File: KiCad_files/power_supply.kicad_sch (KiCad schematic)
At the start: 21 parts, among them Q2 DMP3099L, U7 LTC4412xS6

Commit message: power led
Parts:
- added D1: LED, LED_SMD:LED_0805_2012Metric_Pad1.15x1.40mm_HandSolder, symbol Device:LED
- added R1: 2.2k, Resistor_SMD:R_0805_2012Metric_Pad1.20x1.40mm_HandSolder, symbol Device:R
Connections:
- net +3.3V: now also R1.2
- net GND: now also D1.1 (K)
- new net: D1.2 (A), R1.1
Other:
- moved on the sheet: C17, C18, C19, C20, C21, C25, C26, C5, D2, D3, L5, Q2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

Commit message: digikey field for power supply components
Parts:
- removed L5: SRU1038-5R0Y, Inductor_SMD:L_Bourns-SRU1028_10.0x10.0mm, symbol 1_projektin osat:SRU1038-5R0Y
- added L4: SRU1038-5R0Y, 1_project_library:IND_BOURNS_SRU1038, symbol 1_projektin osat:SRU1038-5R0Y
- C17: DigiKey (none) -> 490-1644-1-ND
- C18, C19, C20: DigiKey (none) -> 720-1754-1-ND
- C21: DigiKey (none) -> 399-C0805C330J5GACTUCT-ND
- C5: DigiKey (none) -> 587-3246-1-ND
- D1: DigiKey (none) -> 492-2281-1-ND
- D2: DigiKey (none) -> CUS10S30H3FCT-ND
- D3: DigiKey (none) -> 1N4148WSFSCT-ND
- Q2: DigiKey (none) -> DMP3099L-7DICT-ND
- R1: DigiKey (none) -> 311-2.20KCRCT-ND
- R10: DigiKey (none) -> 311-100KCRCT-ND
- R11: DigiKey (none) -> 311-20.0CRCT-ND
- R12: DigiKey (none) -> 13-RC0805FR-135K6LCT-ND
- R13: DigiKey (none) -> 13-RT0805FRE0713KLCT-ND
- R14: DigiKey (none) -> 311-40.2KCRCT-ND
- R15: DigiKey (none) -> 311-470KCRCT-ND
- U7: DigiKey (none) -> 505-LTC4412ES6#TRMPBFCT-ND
- U8: DigiKey (none) -> 1589-1573-1-ND
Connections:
- net +3.3V: now also L4.1
- net at C19.1, U8.3 (SW): now also L4.2
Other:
- moved on the sheet: C19, R11

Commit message: c5 korjattu
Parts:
- renumbered C5 to C27
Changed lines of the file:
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@@
 		(dnp no)
 		(fields_autoplaced yes)
-		(property "Reference" "C5"
+		(property "Reference" "C27"
 			(at 231.14 101.5999 0)
 			(effects
@@
 			(project "esp"
 				(path "/186d5500-054c-4b47-a89c-85f6ce2abe33/718dca9f-314d-4628-afec-7956f3606013"
-					(reference "C5")
+					(reference "C27")
 					(unit 1)
 				)

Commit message: johtoja
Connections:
- net VBUS renamed USB_VBUS
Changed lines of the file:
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@@
 	(wire
 		(pts
-			(xy 201.93 95.25) (xy 205.74 95.25)
+			(xy 80.01 72.39) (xy 97.79 72.39)
 		)
 		(stroke
@@
 	(wire
 		(pts
-			(xy 185.42 80.01) (xy 175.26 80.01)
+			(xy 201.93 95.25) (xy 205.74 95.25)
 		)
 		(stroke
@@
 	(wire
 		(pts
-			(xy 218.44 110.49) (xy 227.33 110.49)
+			(xy 185.42 80.01) (xy 175.26 80.01)
 		)
 		(stroke
@@
 	(wire
 		(pts
-			(xy 223.52 81.28) (xy 223.52 95.25)
+			(xy 218.44 110.49) (xy 227.33 110.49)
 		)
 		(stroke
@@
 	(wire
 		(pts
-			(xy 218.44 106.68) (xy 218.44 110.49)
+			(xy 223.52 81.28) (xy 223.52 95.25)
 		)
 		(stroke
@@
 	(wire
 		(pts
-			(xy 124.46 72.39) (xy 124.46 77.47)
+			(xy 218.44 106.68) (xy 218.44 110.49)
 		)
 		(stroke
@@
 	(wire
 		(pts
-			(xy 91.44 72.39) (xy 97.79 72.39)
+			(xy 124.46 72.39) (xy 124.46 77.47)
 		)
 		(stroke
@@
 		)
 	)
+	(hierarchical_label "USB_VBUS"
+		(shape input)
+		(at 80.01 72.39 180)
+		(effects
+			(font
+				(size 1.27 1.27)
+			)
+			(justify right)
+		)
+	)
 	(hierarchical_label "BAT_STAT"
 		(shape output)
@@
 					(unit 1)
 				)
-			)
-		)
-	)
-	(symbol
-		(lib_id "power:VBUS")
-		(at 91.44 72.39 90)
-		(unit 1)
-		(exclude_from_sim no)
-		(in_bom yes)
-		(on_board yes)
-		(dnp no)
-		(fields_autoplaced yes)
-		(property "Reference" "#PWR021"
-			(at 95.25 72.39 0)
-			(effects
-				(font
-					(size 1.27 1.27)
-				)
-				(hide yes)
-			)
-		)
-		(property "Value" "VBUS"
-			(at 87.63 72.3899 90)
-			(effects
-				(font
-					(size 1.27 1.27)
-				)
-				(justify left)
-			)
-		)
-		(property "Footprint" ""
-			(at 91.44 72.39 0)
-			(effects
-				(font
-					(size 1.27 1.27)
-				)
-				(hide yes)
-			)
-		)
-		(property "Datasheet" ""
-			(at 91.44 72.39 0)
-			(effects
-				(font
-					(size 1.27 1.27)
-				)
-				(hide yes)
-			)
-		)
-		(property "Description" "Power symbol creates a global label with name \"VBUS\""
-			(at 91.44 72.39 0)
-			(effects
-				(font
-					(size 1.27 1.27)
-				)
-				(hide yes)
-			)
-		)
-		(pin "1"
-		)
-		(instances
-			(project ""
-				(path "/186d5500-054c-4b47-a89c-85f6ce2abe33/718dca9f-314d-4628-afec-7956f3606013"
-					(reference "#PWR021")
-					(unit 1)
-				)

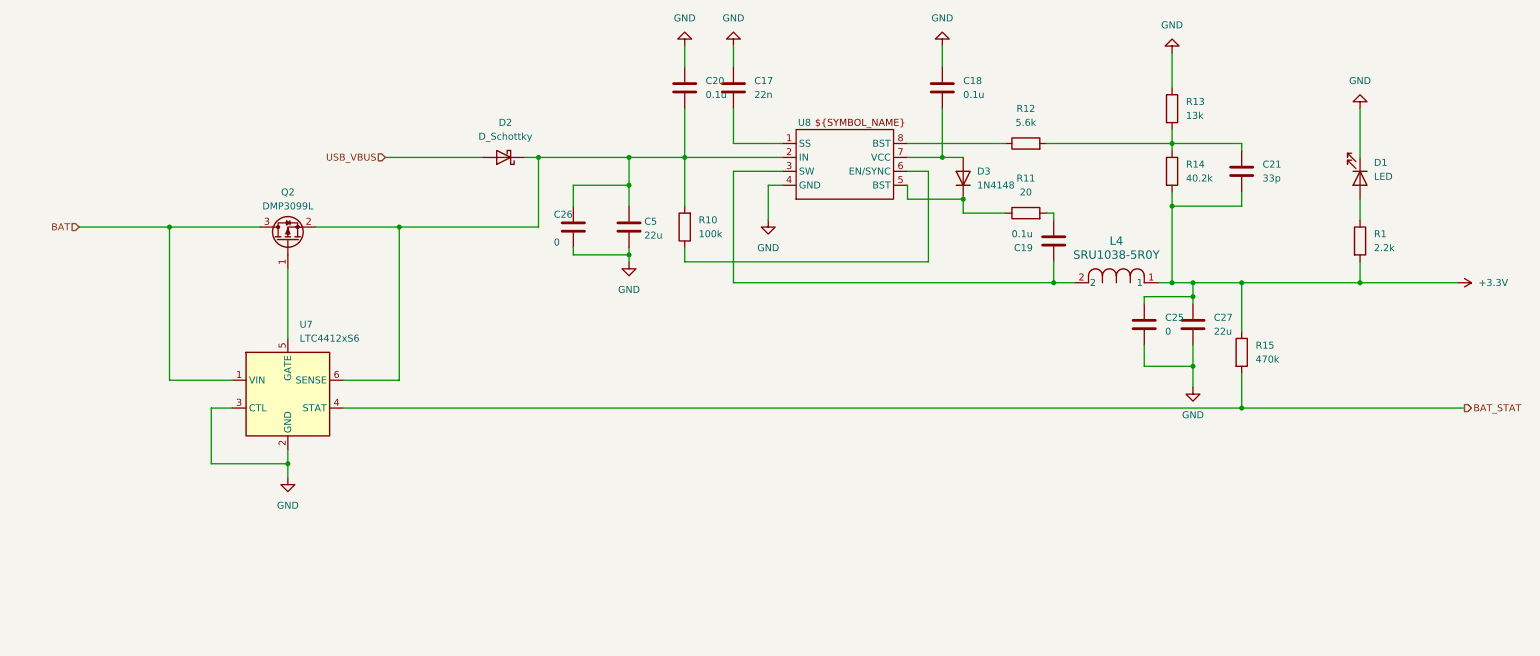
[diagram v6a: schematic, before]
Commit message: dpdt switch
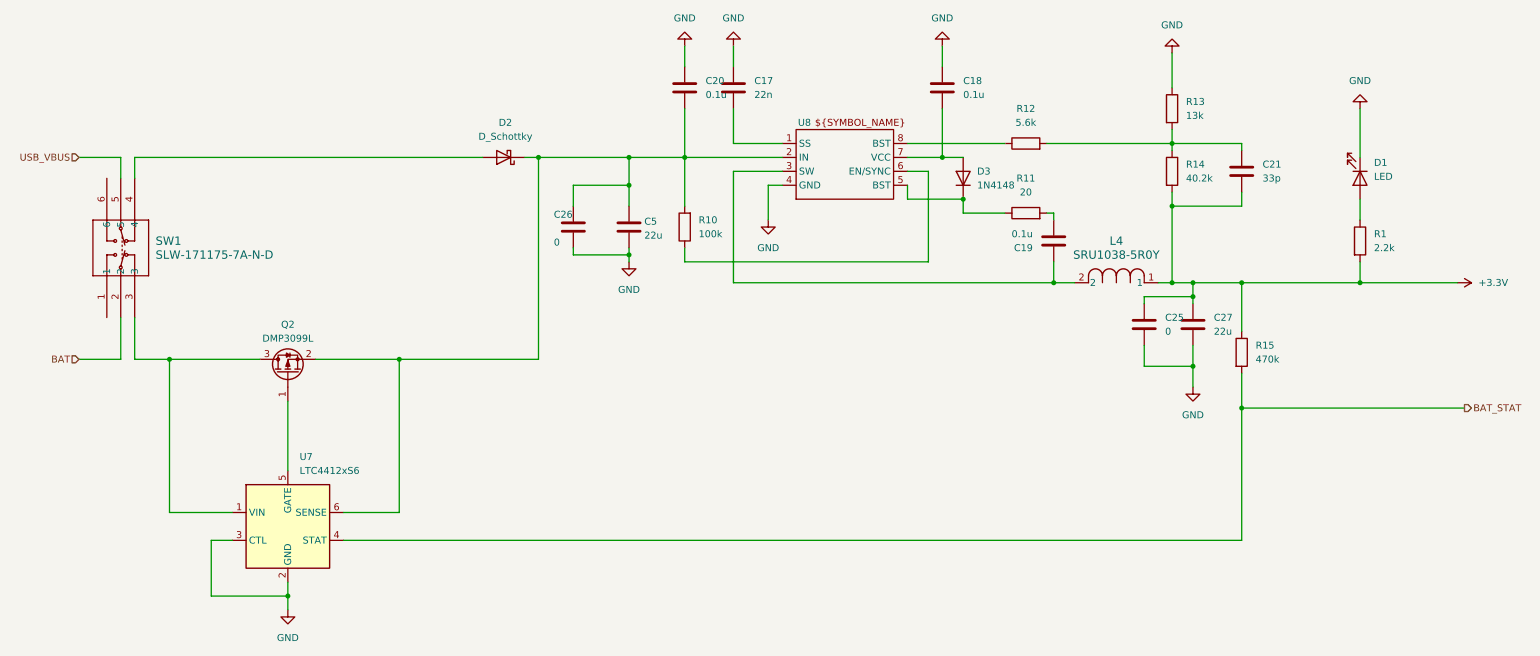
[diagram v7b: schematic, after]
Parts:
- added SW1: SLW-171175-7A-N-D, SLW-171175-7A-N-D_SSD, symbol 1_projektin osat:SLW-171175-7A-N-D
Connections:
- net BAT: now also SW1.2; no longer Q2.3 (D), U7.1 (VIN)
- net USB_VBUS: now also SW1.5; no longer D2.2 (A)
- new net: Q2.3 (D), SW1.3, U7.1 (VIN)
- new net: D2.2 (A), SW1.4
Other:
- moved on the sheet: Q2, U7

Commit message: ERC hiljennetty
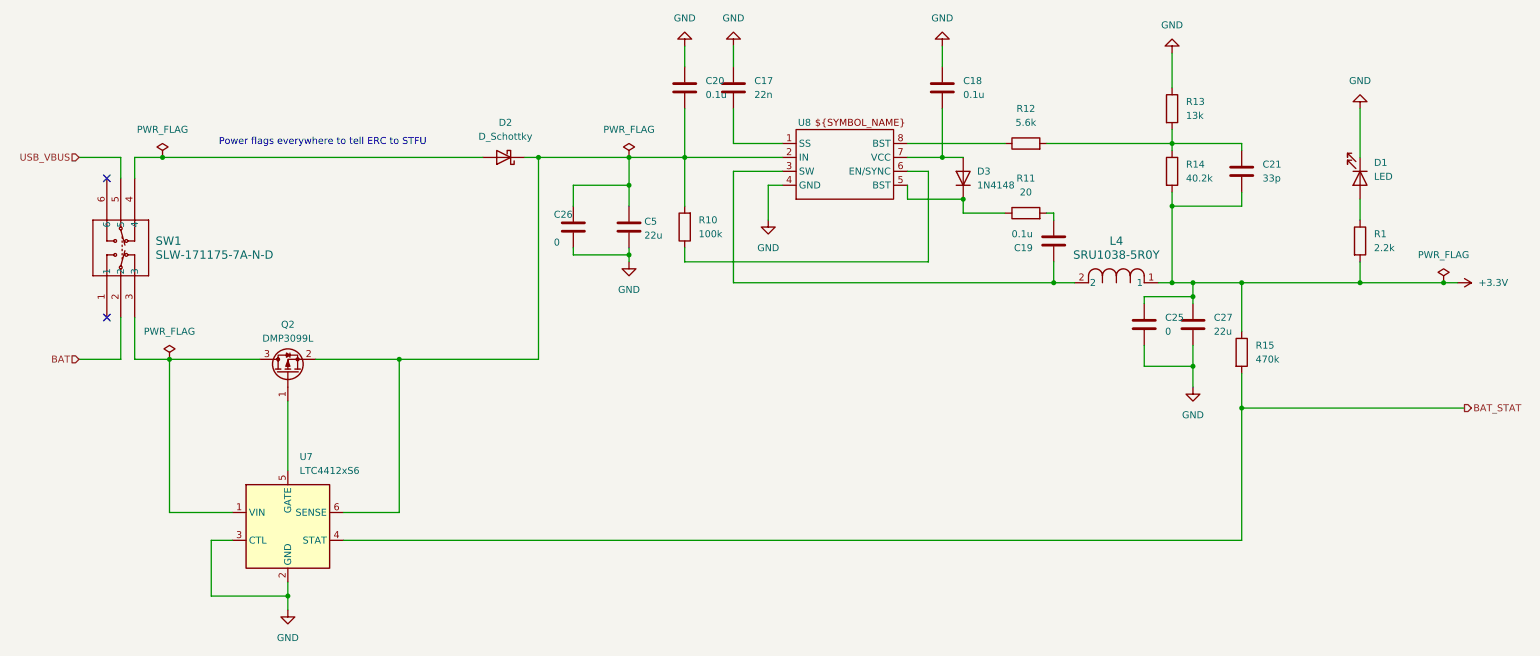
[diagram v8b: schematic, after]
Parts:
- SW1: footprint SLW-171175-7A-N-D_SSD -> 1_project_library:SLW-171175-7A-N-D_SSD; DigiKey 2223-SLW-171175-7A-N-D-ND -> 2223-SLW-171175-7A-N-D-ND
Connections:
- no-connect marks 0 -> 2
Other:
- note added: "Power flags everywhere to tell ERC to STFU"
